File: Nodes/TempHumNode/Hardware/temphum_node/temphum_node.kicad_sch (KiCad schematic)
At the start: 37 parts, among them IC1 CC1310F128RGZR, IC2 TPD6E004RSER, J1 TC2050-IDC, U1 MCP73123-22SI/MF, Y2 TSX-3225 24.0000MF15X-AC3, Y3 FC-135_32.7680KA-AG0

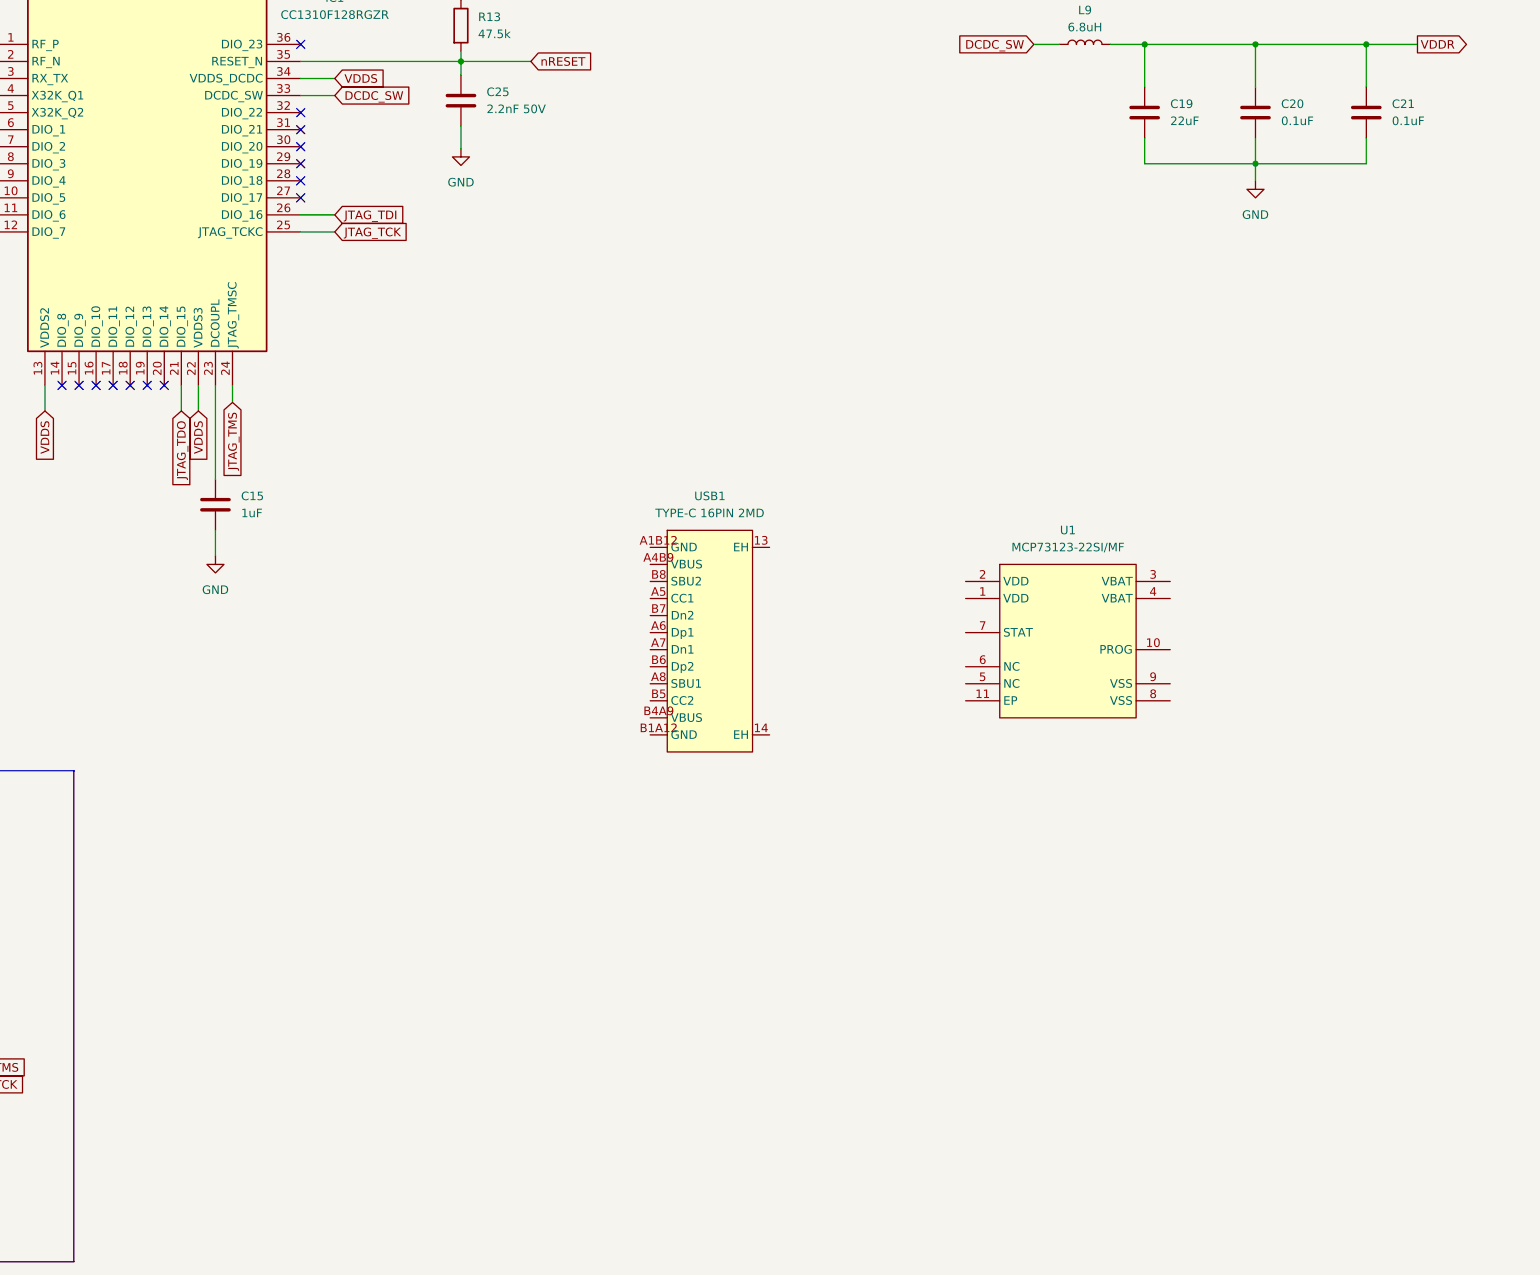
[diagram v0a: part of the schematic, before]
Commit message: hw(temphum-node): add SHT35 (custom symbol layout) + schematic/board progress
Import SHT35-DIS-B (LCSC C90161) footprint + 3D model, and swap the
symbol graphics for the user's custom pin arrangement from the
temperatureSensorSubGHz project (keeps footprint link + LCSC/BOM
fields). Plus in-progress schematic/board work.

Co-Authored-By: Claude Opus 4.8 (1M context) <noreply@anthropic.com>
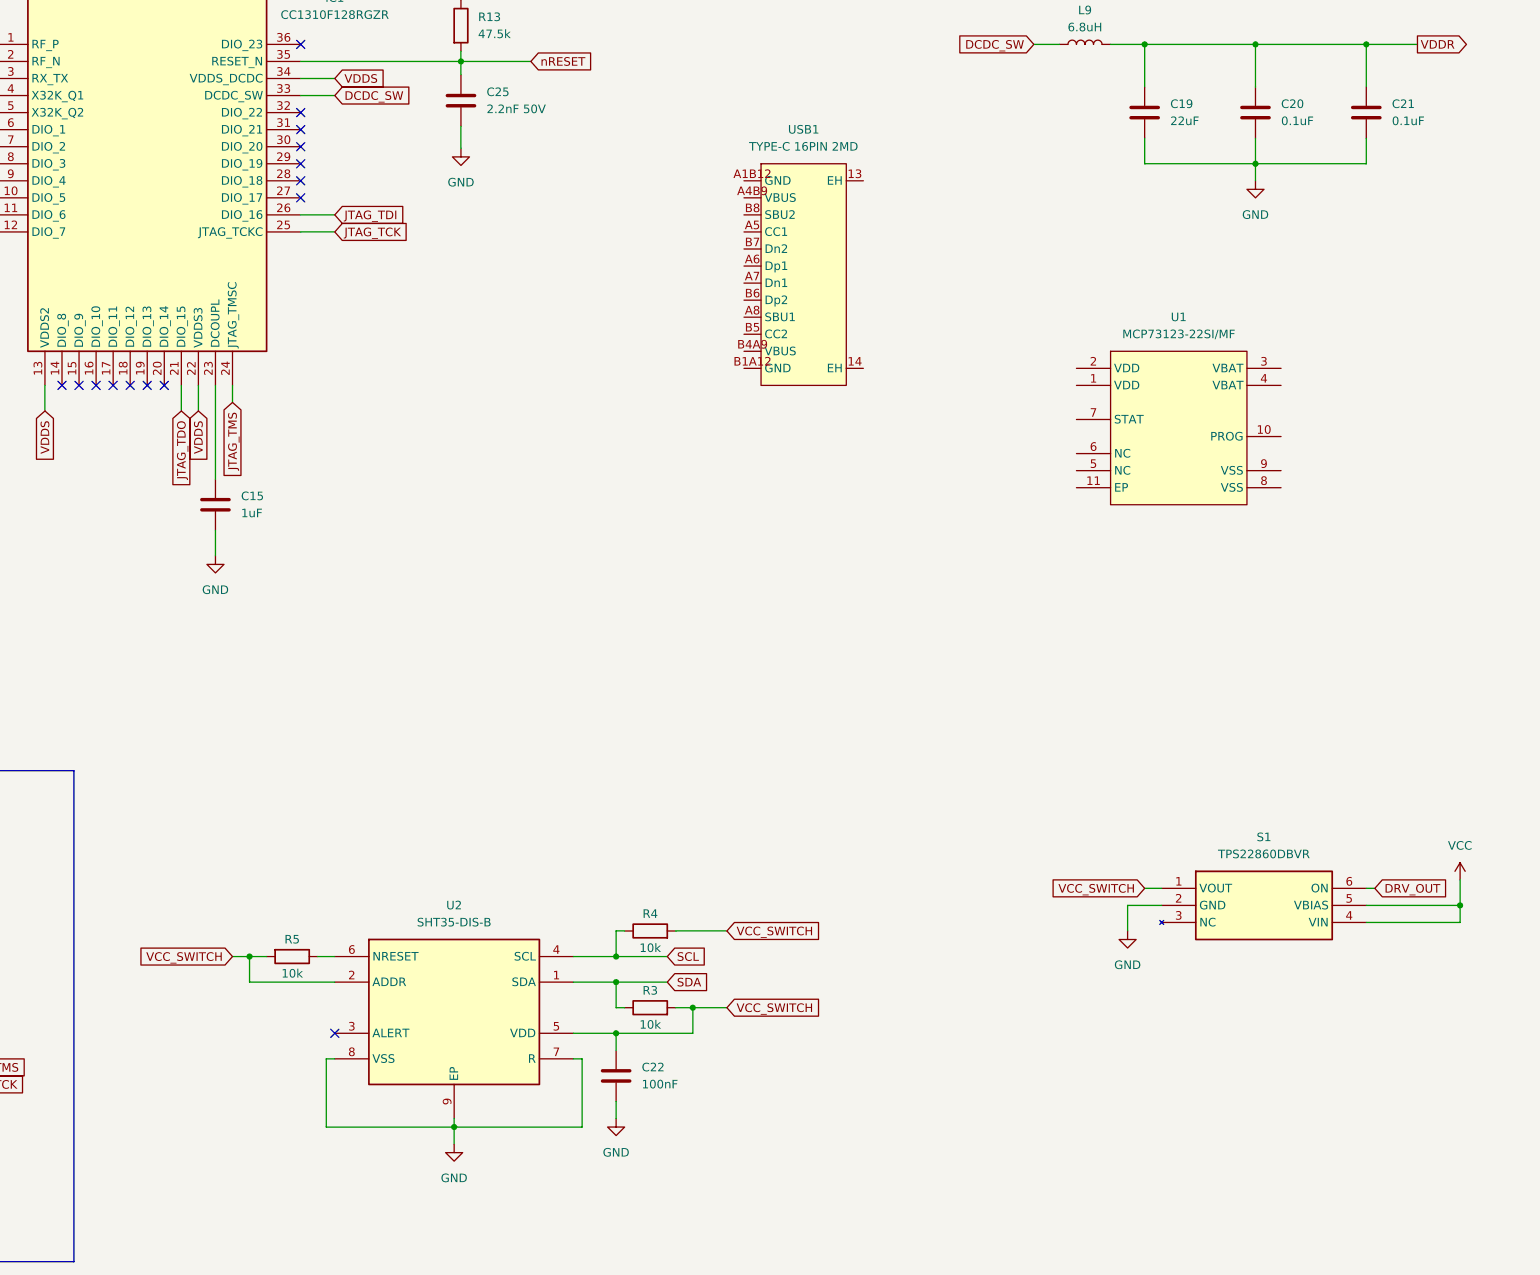
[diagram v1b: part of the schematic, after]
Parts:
- added C22: 100nF, CC0603KRX7R9BB104:CAPC1608X90N, symbol Device:C
- added R3, R4, R5: 10k, CRCW060310K0FKEA:RESC1608X50N, symbol Device:R
- added S1: TPS22860DBVR, SOT95P280X145-6N, symbol TPS22860DBVR:TPS22860DBVR
- added U2: SHT35-DIS-B, SmartHome:DFN-8_L2.5-W2.5-P0.50-TL-EP, symbol SmartHome:SHT35-DIS-B
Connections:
- net GND: now also C22.2, S1.2 (GND), U2.7 (R), U2.8 (VSS), U2.9 (EP)
- new net: R5.1, U2.6 (NRESET)
- new net DRV_OUT: S1.6 (ON)
- new net SCL: R4.1, U2.4 (SCL)
- new net SDA: R3.1, U2.1 (SDA)
- new net VCC: S1.4 (VIN), S1.5 (VBIAS)
- new net VCC_SWITCH: C22.1, R3.2, R4.2, R5.2, S1.1 (VOUT), U2.2 (ADDR), U2.5 (VDD)
- no-connect marks 26 -> 27
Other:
- moved on the sheet: U1, USB1

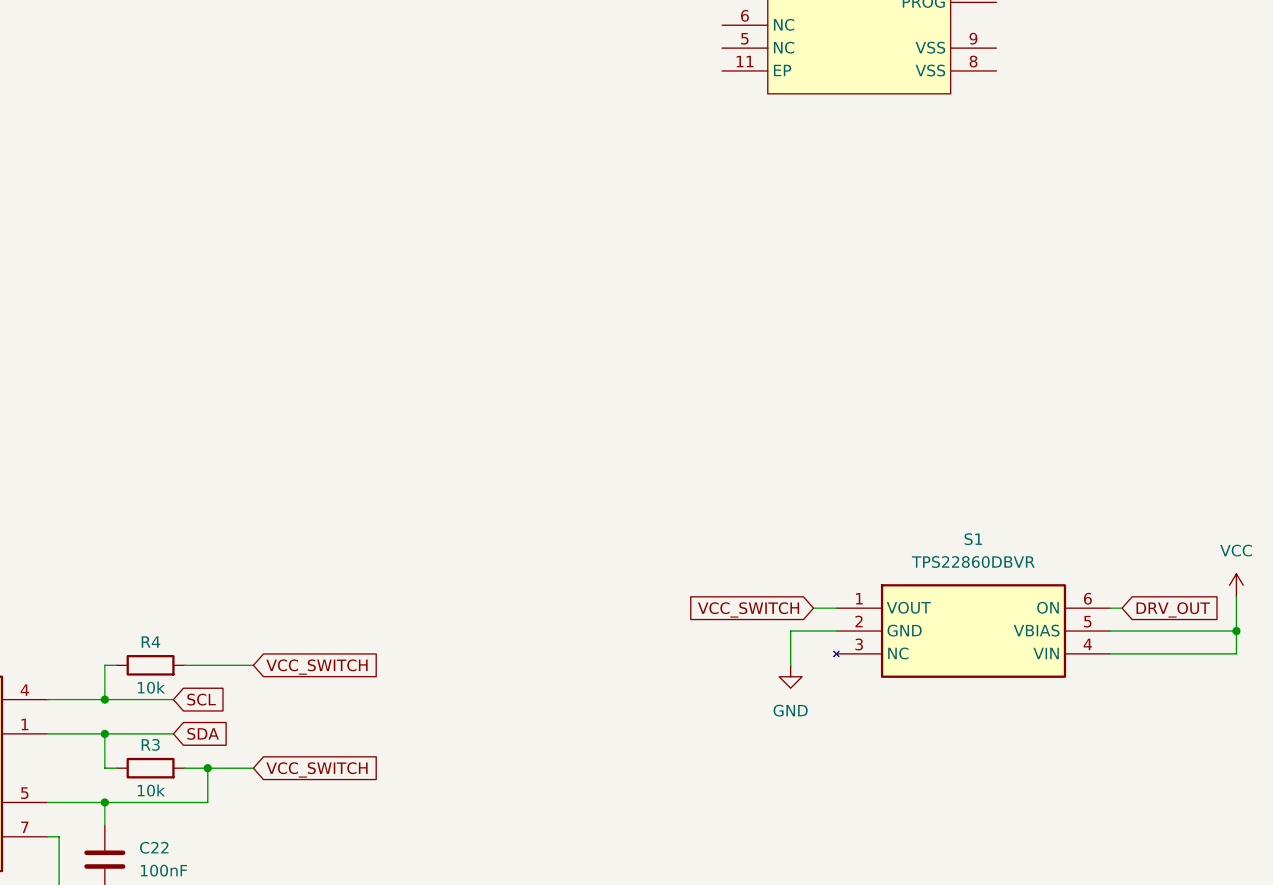
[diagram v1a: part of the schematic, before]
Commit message: hw(temphum-node): add power/protection parts (TPS63900, MCP3421, TPS22860, PCM)
Import LDO/converter TPS63900 (buck-boost 3.3V), MCP3421A0 (18-bit ADC,
I2C 0x68 for battery SoC), TPS22860 (load switch), and the LiFePO4 PCM
pair HY2112 + FS8205A. Footprints/symbols/3D into Shared/KiCadLib.

Co-Authored-By: Claude Opus 4.8 (1M context) <noreply@anthropic.com>
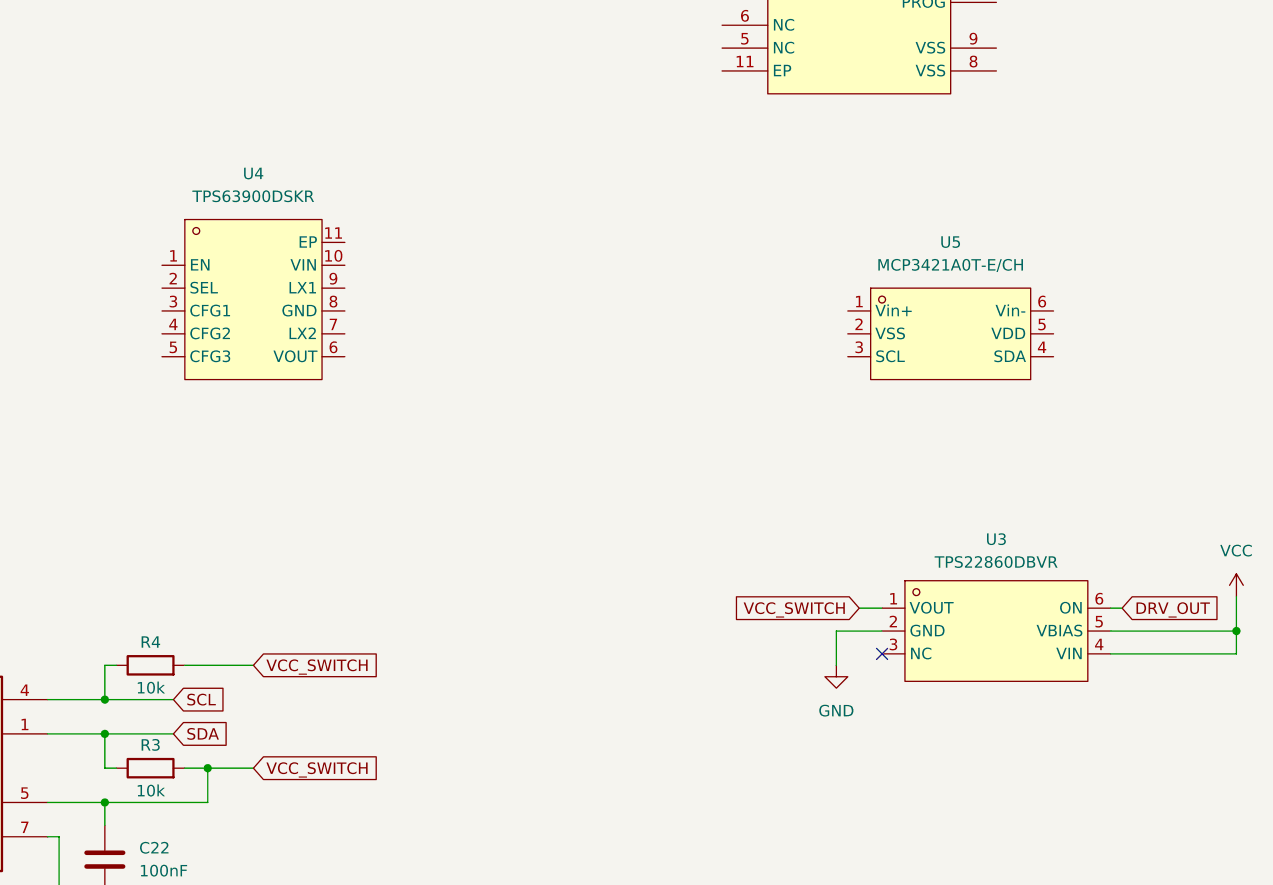
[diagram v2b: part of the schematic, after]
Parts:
- removed S1: TPS22860DBVR, SOT95P280X145-6N, symbol TPS22860DBVR:TPS22860DBVR
- added U3: TPS22860DBVR, SmartHome:SOT-23-6_L2.9-W1.6-P0.95-LS2.8-BR, symbol SmartHome:TPS22860DBVR
- added U4: TPS63900DSKR, SmartHome:WSON-10_L2.5-W2.5-W0.50-TL-EP, symbol SmartHome:TPS63900DSKR
- added U5: MCP3421A0T-E/CH, SmartHome:SOT-23-6_L2.9-W1.6-P0.95-LS2.8-BR, symbol SmartHome:MCP3421A0T-E_CH
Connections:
- net DRV_OUT: now also U3.6 (ON)
- net GND: now also U3.2 (GND)
- net VCC: now also U3.4 (VIN), U3.5 (VBIAS)
- net VCC_SWITCH: now also U3.1 (VOUT)
- no-connect marks 27 -> 28
